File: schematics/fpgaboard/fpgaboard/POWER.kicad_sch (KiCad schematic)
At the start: 4 parts, among them U2 AMS1117-3.3

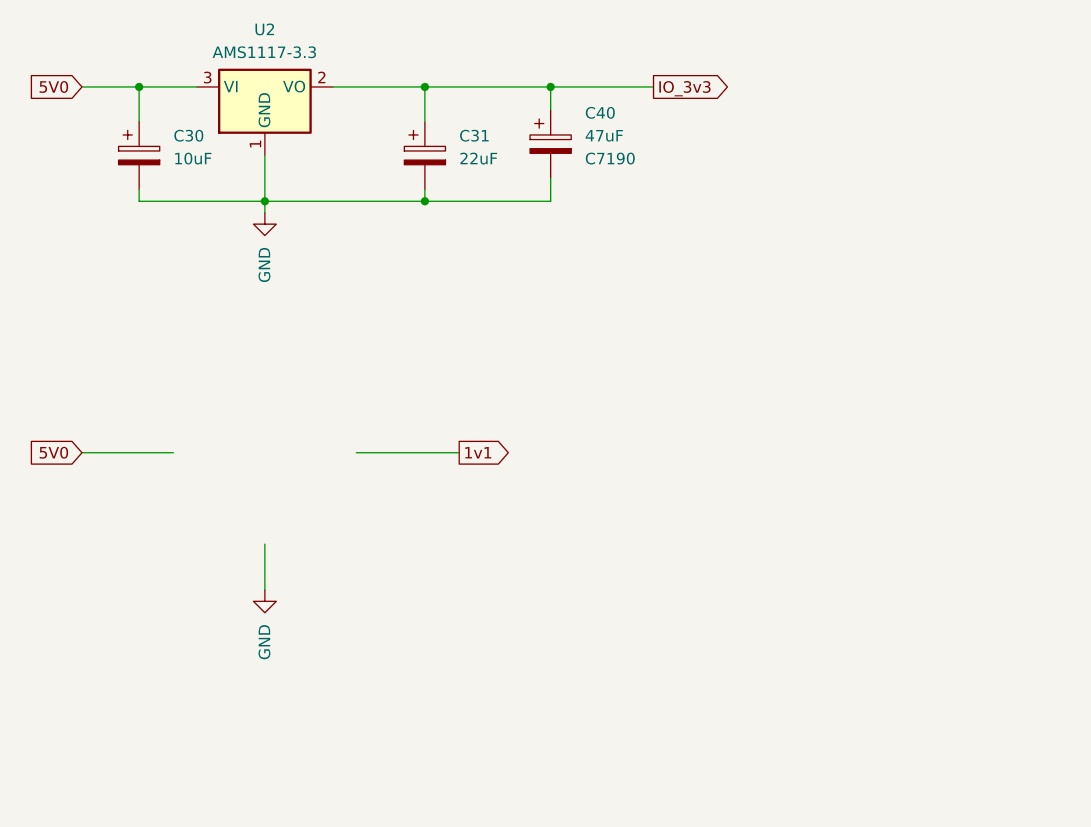
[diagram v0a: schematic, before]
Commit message: Work on connecting up SDRAM to FPGA.
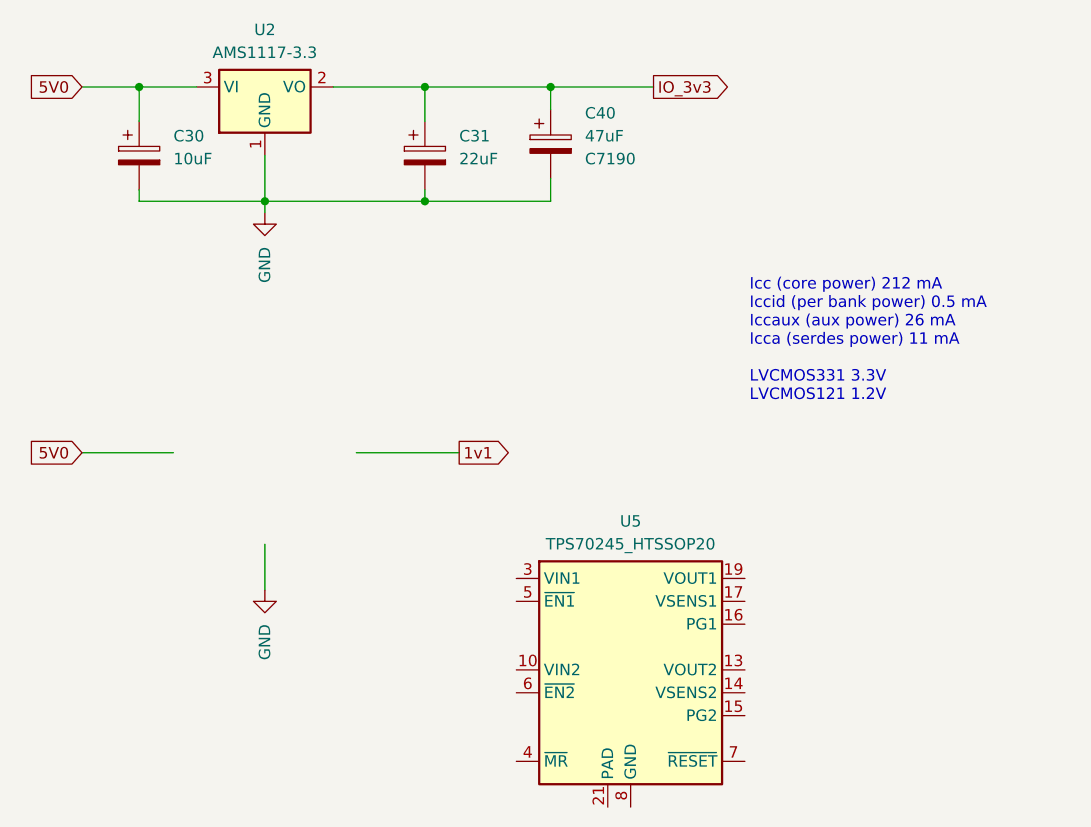
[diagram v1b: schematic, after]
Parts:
- added U5: TPS70245_HTSSOP20, Package_SO:HTSSOP-20-1EP_4.4x6.5mm_P0.65mm_EP3.4x6.5mm_ThermalVias, symbol Regulator_Linear:TPS70245_HTSSOP20
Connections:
- new net: U5.10 (VIN2), U5.9 (VIN2)
- new net: U5.12 (VOUT2), U5.13 (VOUT2)
- new net: U5.18 (VOUT1), U5.19 (VOUT1)
- new net: U5.2 (VIN1), U5.3 (VIN1)
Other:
- note added: "Icc (core power) 212 mA Iccid (per bank power) 0.5 mA Iccaux (aux power) 26 mA Icca (serdes power) 11 mA LVCMOS331 3.3V LVCMOS121 1.2V"
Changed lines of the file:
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@@
 	(generator_version "9.0")
 	(paper "A4")
+	(text "Icc (core power) 212 mA\nIccid (per bank power) 0.5 mA\nIccaux (aux power) 26 mA\nIcca (serdes power) 11 mA\n\nLVCMOS331 3.3V\nLVCMOS121 1.2V\n"
+		(exclude_from_sim no)
+		(at 146.558 90.424 0)
+		(effects
+			(font
+				(size 1.27 1.27)
+			)
+			(justify left)
+		)
+	)
 	(junction
 		(at 110.49 74.93)
@@
 					(unit 1)
 				)
+			)
+		)
+	)
+	(symbol
+		(lib_id "Regulator_Linear:TPS70245_HTSSOP20")
+		(at 133.35 127 0)
+		(unit 1)
+		(exclude_from_sim no)
+		(in_bom yes)
+		(on_board yes)
+		(dnp no)
+		(fields_autoplaced yes)
+		(property "Reference" "U5"
+			(at 133.35 110.49 0)
+			(effects
+				(font
+					(size 1.27 1.27)
+				)
+			)
+		)
+		(property "Value" "TPS70245_HTSSOP20"
+			(at 133.35 113.03 0)
+			(effects
+				(font
+					(size 1.27 1.27)
+				)
+			)
+		)
+		(property "Footprint" "Package_SO:HTSSOP-20-1EP_4.4x6.5mm_P0.65mm_EP3.4x6.5mm_ThermalVias"
+			(at 132.715 111.125 0)
+			(effects
+				(font
+					(size 1.27 1.27)
+					(italic yes)
+				)
+				(hide yes)
+			)
+		)
+		(property "Datasheet" "http://www.ti.com/lit/ds/symlink/tps702.pdf"
+			(at 133.35 134.62 0)
+			(effects
+				(font
+					(size 1.27 1.27)
+				)
+				(hide yes)
+			)
+		)
+		(property "Description" "3.3V 500mA/1.2V 250mA Dual Low Drop-out Regulator with Voltage Supervisor, PowerPAD TSSOP-20"
+			(at 133.35 127 0)
+			(effects
+				(font
+					(size 1.27 1.27)
+				)
+				(hide yes)
+			)
+		)
+		(pin "10"
+		)
+		(pin "17"
+		)
+		(pin "15"
+		)
+		(pin "6"
+		)
+		(pin "14"
+		)
+		(pin "1"
+		)
+		(pin "2"
+		)
+		(pin "19"
+		)
+		(pin "5"
+		)
+		(pin "8"
+		)
+		(pin "20"
+		)
+		(pin "9"
+		)
+		(pin "11"
+		)
+		(pin "21"
+		)
+		(pin "18"
+		)
+		(pin "12"
+		)
+		(pin "13"
+		)
+		(pin "3"
+		)
+		(pin "4"
+		)
+		(pin "16"
+		)
+		(pin "7"
+		)
+		(instances
+			(project ""
+				(path "/a85e5c81-2db0-4fec-8ba8-fa5236bf3fa2/4611da13-b1b8-49fc-bb4a-1e9970e119a4"
+					(reference "U5")
+					(unit 1)
+				)
